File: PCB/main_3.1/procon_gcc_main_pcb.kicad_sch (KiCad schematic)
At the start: 130 parts, among them J1 Conn_01x04_Pin, J2 SM02B-SURS-TF_LF__SN_, J3 To Button Board, J4 SM02B-SURS-TF_LF__SN_, J5 Conn_01x02_Pin, J9 USB_C_Receptacle, Q4 BSS138DW, Q5 BSS138DW, Q7 MMBT3904, Q8 MMBT3904, SW1 1TS026A-1000-0550, SW1 GL18_SW, SW2 GL18_SW, SW4 TS35CA, T1 36-8730, T2 36-8730, T3 36-8730, T4 36-8730, U1 GH39F (Hall SOT23), U10 MCP3002, U11 ST_LSM6, U12 PI3USB4000A, U15 DRV2605LYZFR, U16 BQ25180, U2 GD25Q80EEIGR, U2 GH39F (Hall SOT23), U3 GH39F (Hall SOT23), U4 GH39F (Hall SOT23), U4 TPS630001RCR, U5 ST_LSM6, U6 RP2040, U7 CH340K, U8 MCP3002, U9 ESP32-PICO-MINI-02, Y1 Crystal_GND3

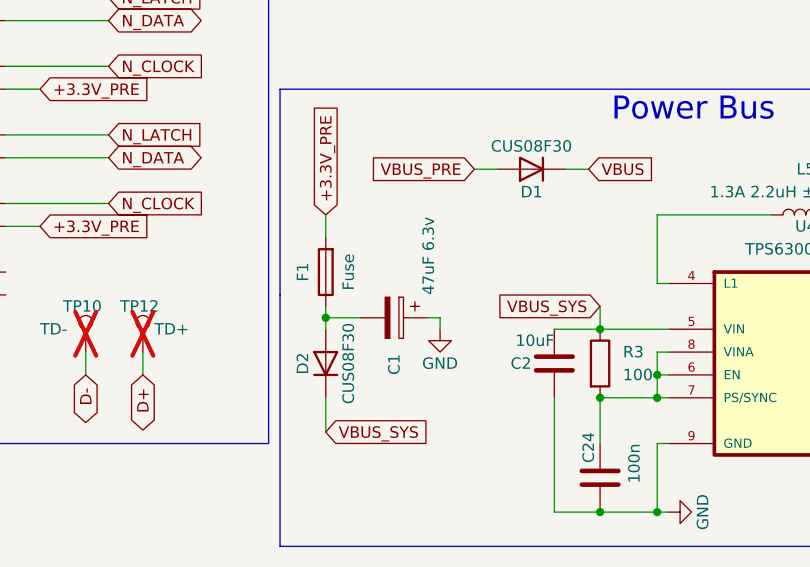
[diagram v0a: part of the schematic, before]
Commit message: PCB and FW Updates
- Add player number support internally
- Add debug for bt baseband updating
- Orange indication for baseband update mode
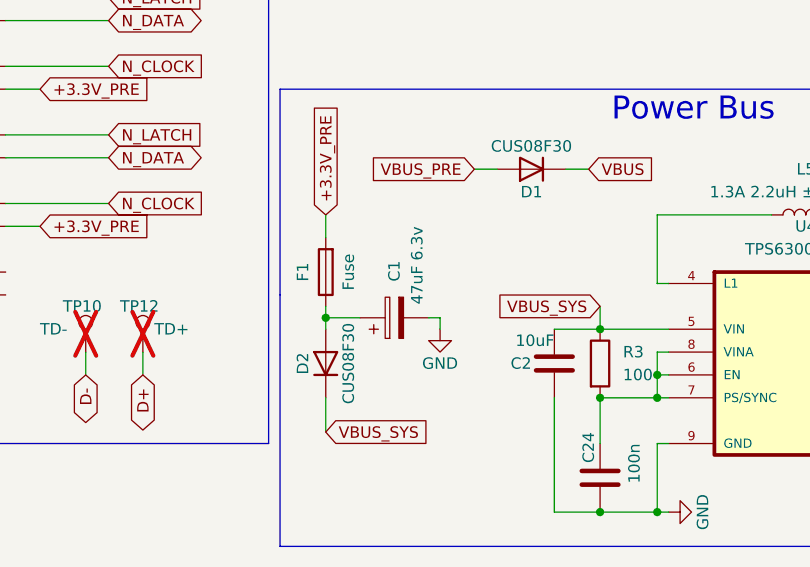
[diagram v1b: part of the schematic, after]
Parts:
- U12: USBDNP (none) -> YES
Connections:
- net GND: now also C1.2; no longer C1.1
- net at D2.2 (A), F1.1: now also C1.1; no longer C1.2
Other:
- moved on the sheet: C1
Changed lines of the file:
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@@
       (effects (font (size 1.27 1.27)) hide)
     )
-    (property "USBDNP" "" (at -121.92 210.82 0)
+    (property "USBDNP" "YES" (at -121.92 210.82 0)
       (effects (font (size 1.27 1.27)) hide)
     )
@@
     )
   )
-  (symbol (lib_id "Device:C_Polarized") (at 86.36 176.53 270) (unit 1)
-    (in_bom yes) (on_board yes) (dnp no)
-    (property "Reference" "C1" (at 86.36 182.88 0)
+  (symbol (lib_id "Device:C_Polarized") (at 86.36 176.53 90) (unit 1)
+    (in_bom yes) (on_board yes) (dnp no)
+    (property "Reference" "C1" (at 86.36 170.18 0)
       (effects (font (size 1.27 1.27)) (justify right))
     )
-    (property "Value" "47uF 6.3v" (at 90.17 173.99 0)
+    (property "Value" "47uF 6.3v" (at 88.9 166.37 0)
       (effects (font (size 1.27 1.27)) (justify right))
     )
-    (property "Footprint" "Capacitor_Tantalum_SMD:CP_EIA-3216-18_Kemet-A" (at 82.55 177.4952 0)
-      (effects (font (size 1.27 1.27)) hide)
-    )
+    (property "Footprint" "Capacitor_Tantalum_SMD:CP_EIA-3216-18_Kemet-A" (at 90.17 175.5648 0)
+      (effects (font (size 1.27 1.27)) hide)
+    )

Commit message: 5.16.2024 update
N64 Fixes
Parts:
- removed F1: Fuse, Fuse:Fuse_1206_3216Metric_Pad1.42x1.75mm_HandSolder, symbol Device:Fuse
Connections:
- net +3.3V_PRE: now also C1.1, D2.2 (A)
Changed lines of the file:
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@@
     (stroke (width 0) (type default))
   )
-  (wire (pts (xy 78.74 165.1) (xy 78.74 167.64))
+  (wire (pts (xy 78.74 173.99) (xy 78.74 176.53))
     (stroke (width 0) (type default))
   )
@@
     (stroke (width 0) (type default))
   )
-  (wire (pts (xy 78.74 175.26) (xy 78.74 176.53))
-    (stroke (width 0) (type default))
-  )
   (wire (pts (xy 176.53 246.38) (xy 176.53 251.46))
     (stroke (width 0) (type default))
@@
     )
   )
-  (global_label "+3.3V_PRE" (shape input) (at 78.74 165.1 90) (fields_autoplaced)
+  (global_label "+3.3V_PRE" (shape input) (at 78.74 173.99 90) (fields_autoplaced)
     (effects (font (size 1.27 1.27)) (justify left))
-    (property "Intersheetrefs" "${INTERSHEET_REFS}" (at 78.74 152.4276 90)
+    (property "Intersheetrefs" "${INTERSHEET_REFS}" (at 78.74 161.3176 90)
       (effects (font (size 1.27 1.27)) (justify left) hide)
     )
@@
         )
       )
-    )
-  )
-  (symbol (lib_id "Device:Fuse") (at 78.74 171.45 180) (unit 1)
-    (in_bom yes) (on_board yes) (dnp no)
-    (property "Reference" "F1" (at 76.2 171.45 90)
-      (effects (font (size 1.27 1.27)))
-    )
-    (property "Value" "Fuse" (at 81.28 171.45 90)
-      (effects (font (size 1.27 1.27)))
-    )
-    (property "Footprint" "Fuse:Fuse_1206_3216Metric_Pad1.42x1.75mm_HandSolder" (at 80.518 171.45 90)
-      (effects (font (size 1.27 1.27)) hide)
-    )
-    (property "Datasheet" "~" (at 78.74 171.45 0)
-      (effects (font (size 1.27 1.27)) hide)
-    )
-    (property "LCSC" "C69680" (at 78.74 171.45 0)
-      (effects (font (size 1.27 1.27)) hide)
-    )
-    (property "MPN" "" (at 78.74 171.45 0)
-      (effects (font (size 1.27 1.27)) hide)
-    )
-    (property "Manufacturer" "" (at 78.74 171.45 0)
-      (effects (font (size 1.27 1.27)) hide)
-    )
-    (pin "1")
-    (pin "2")
-    (instances
-      (project "GCP-2"
-        (path "/066be9b8-34d2-4336-ae00-5e5ce007fbe1"
-          (reference "F1") (unit 1)
-        )
-      )
-      (project "procon_gcc_main_pcb"
-        (path "/9ec9c1c0-f5f6-4920-ad47-c5d4aa989114"
-          (reference "F2") (unit 1)
-        )
-      )
